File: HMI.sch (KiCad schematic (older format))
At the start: 42 parts, among them J24 Display, J25 SPI Interface, J26 I2C Interface, J27 LED4, J28 LED3, J29 Key 3, J30 Key 4, J31 Key 1, J32 Key 2, Q8 BC817, Q9 BC817, U9 74HC245

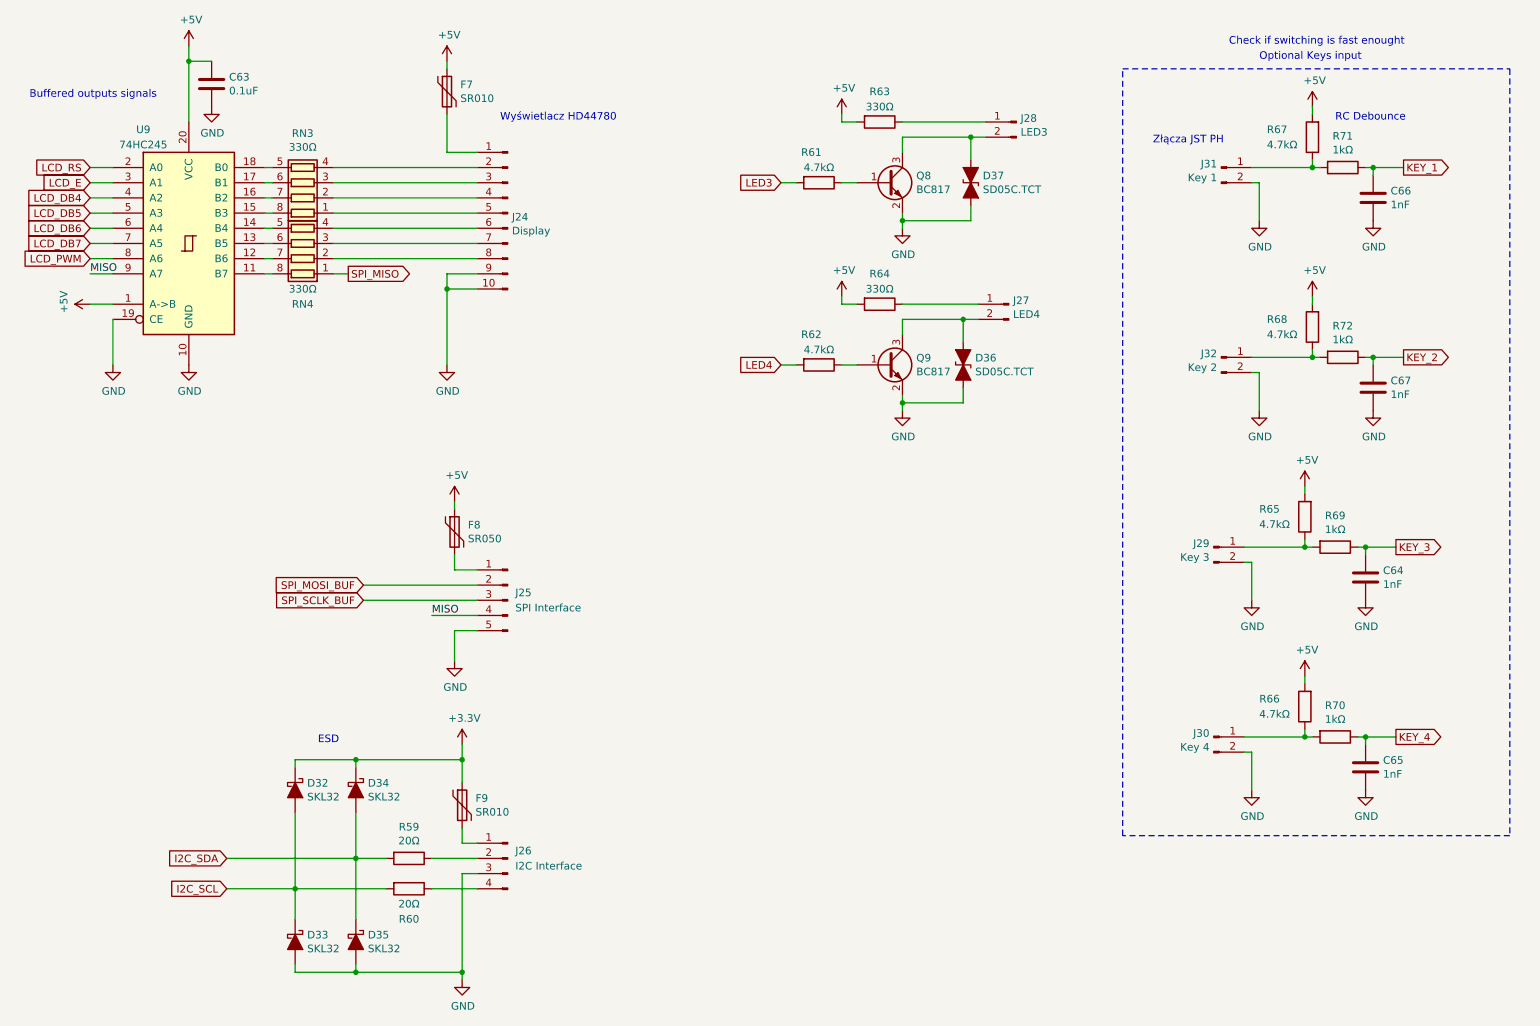
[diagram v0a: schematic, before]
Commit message: Added 12V regulator, aditional input, outputs, improved inputs ESD
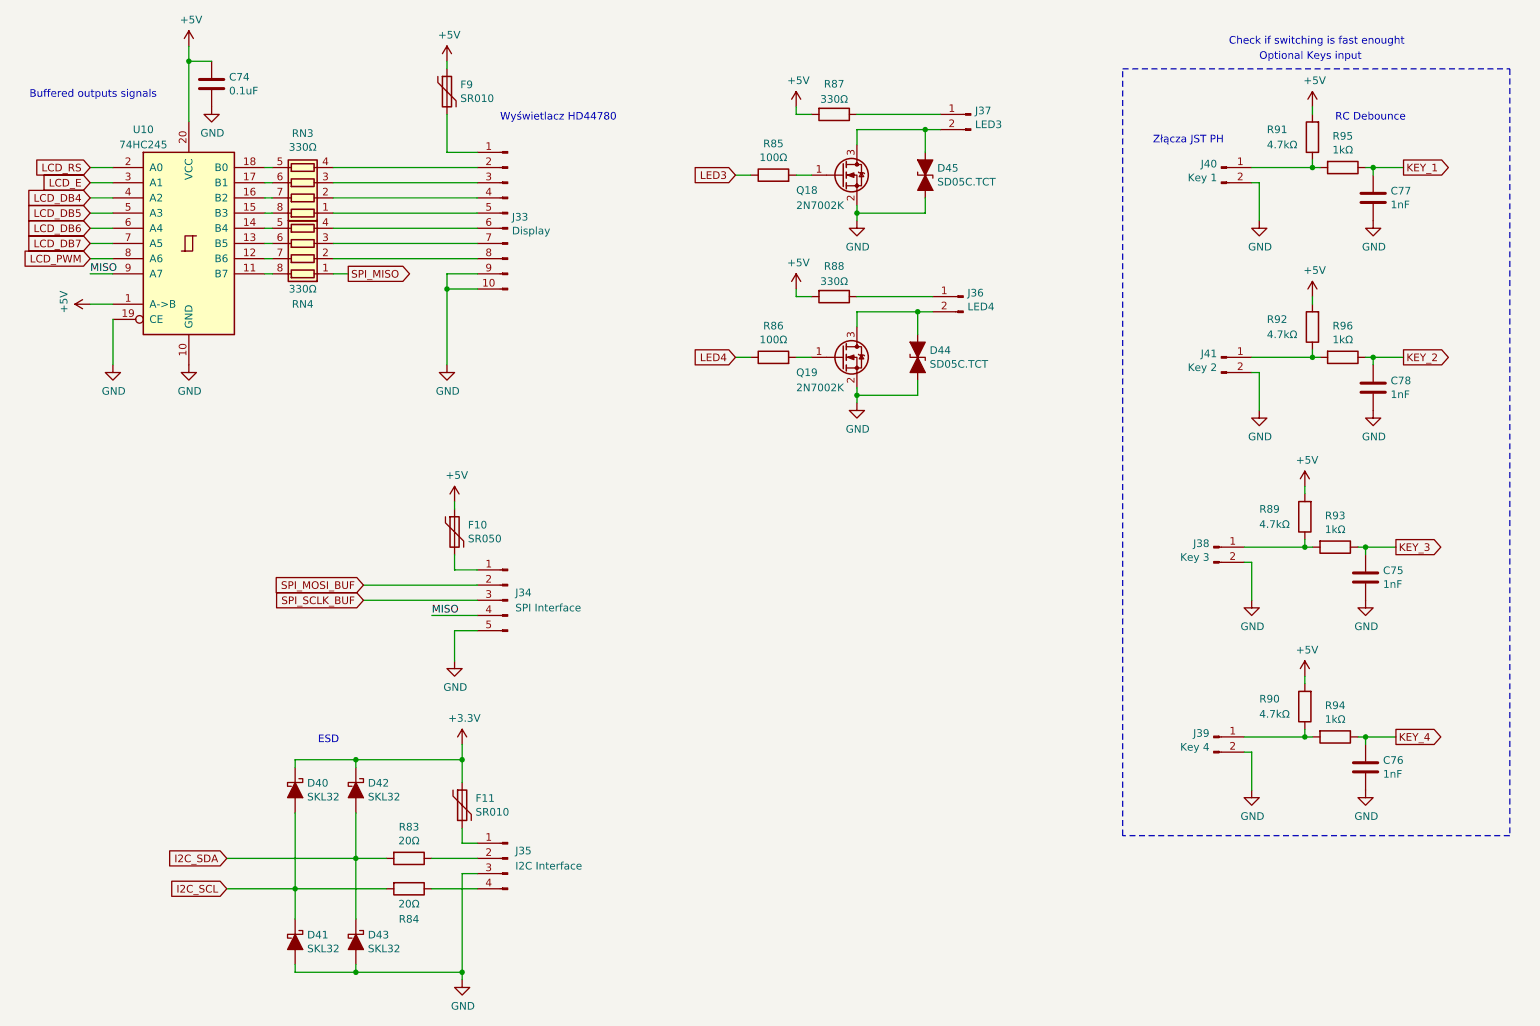
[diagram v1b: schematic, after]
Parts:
- removed Q8, Q9: BC817, Package_TO_SOT_SMD:SOT-23, symbol Transistor_BJT:BC817
- removed R61, R62: 4.7kΩ, Resistor_SMD:R_0603_1608Metric, symbol Device:R
- added Q18, Q19: 2N7002K, Package_TO_SOT_SMD:SOT-23, symbol Transistor_FET:2N7002K
- added R85, R86: 100Ω, Resistor_SMD:R_0603_1608Metric, symbol Device:R
- renumbered C63 to C74, C64 to C75, C65 to C76, C66 to C77, C67 to C78, D32 to D40, D33 to D41, D34 to D42, D35 to D43, D36 to D44, D37 to D45, F8 to F10, F9 to F11, F7 to F9, J24 to J33, J25 to J34, J26 to J35, J27 to J36, J28 to J37, J29 to J38, J30 to J39, J31 to J40, J32 to J41, R59 to R83, R60 to R84, R63 to R87, R64 to R88, R65 to R89, R66 to R90, R67 to R91, R68 to R92, R69 to R93, R70 to R94, R71 to R95, R72 to R96, U9 to U10
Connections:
- net GND: now also Q18.2 (S), Q19.2 (S)
- net LED3: now also R85.1
- net LED4: now also R86.1
- net at D45.1 (A1), J37.2 (Pin_2): now also Q18.3 (D)
- net at D44.1 (A1), J36.2 (Pin_2): now also Q19.3 (D)
- new net: Q19.1 (G), R86.2
- new net: Q18.1 (G), R85.2
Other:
- moved on the sheet: D44, D45, J36, J37, R87, R88

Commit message: Added analog input
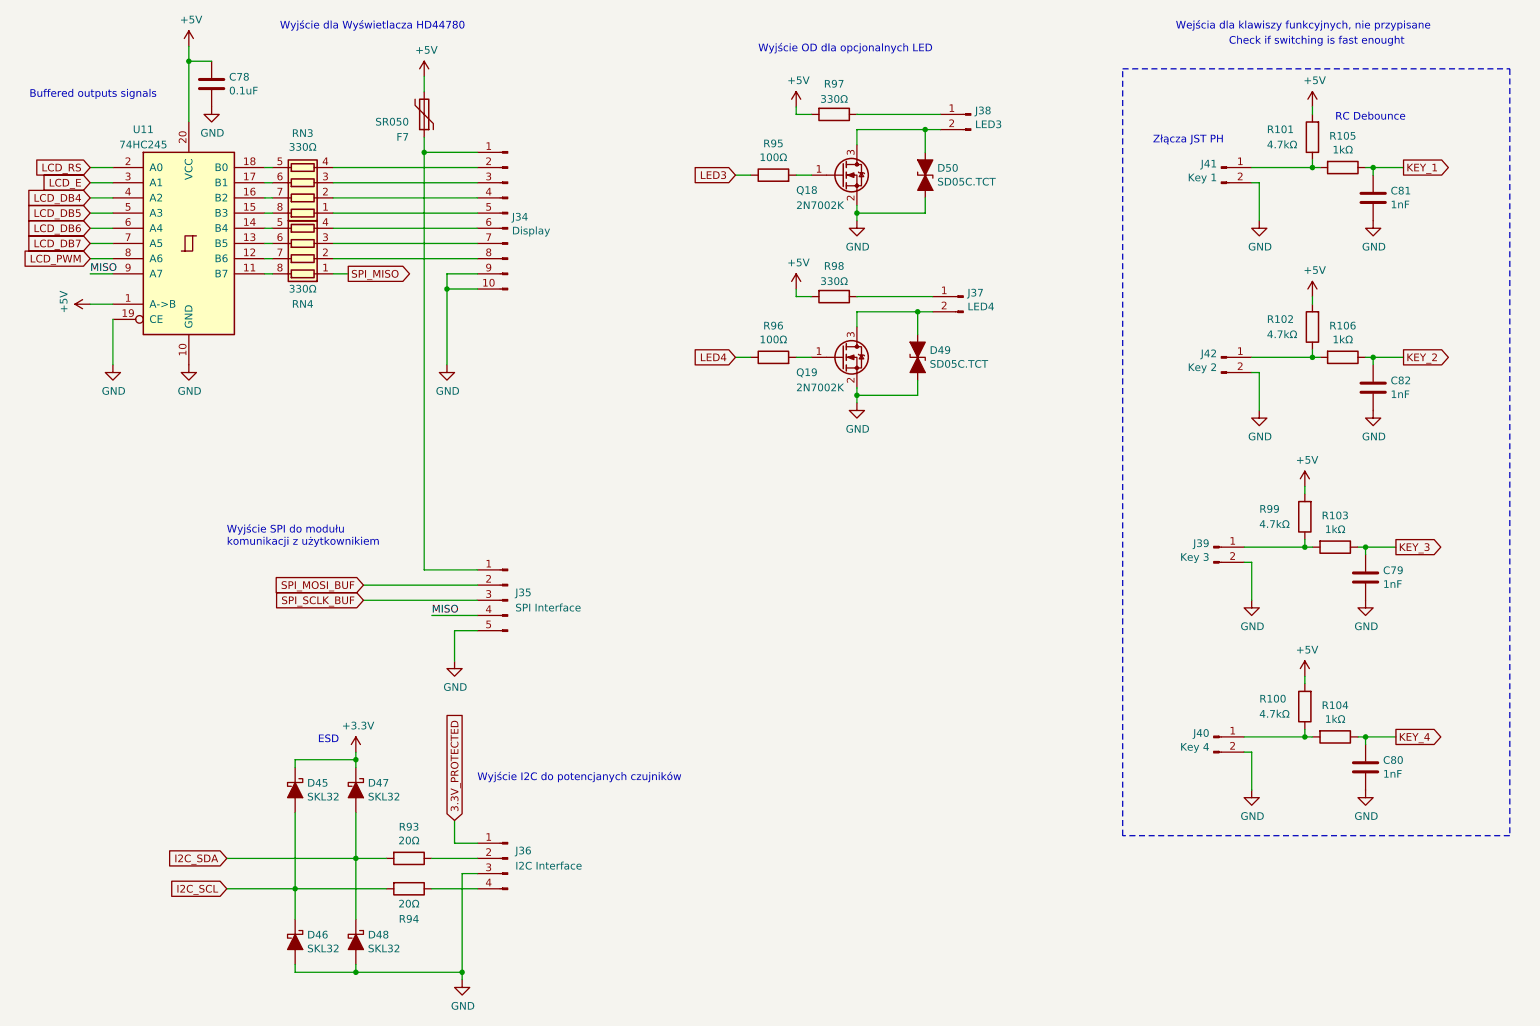
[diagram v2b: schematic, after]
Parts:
- removed F10: SR050, Fuse:Fuse_0805_2012Metric, symbol Device:Polyfuse
- removed F11, F9: SR010, Fuse:Fuse_0805_2012Metric, symbol Device:Polyfuse
- added F7: SR050, Fuse:Fuse_0805_2012Metric, symbol Device:Polyfuse
- renumbered C74 to C78, C75 to C79, C76 to C80, C77 to C81, C78 to C82, D40 to D45, D41 to D46, D42 to D47, D43 to D48, D44 to D49, D45 to D50, J33 to J34, J34 to J35, J35 to J36, J36 to J37, J37 to J38, J38 to J39, J39 to J40, J40 to J41, J41 to J42, R90 to R100, R91 to R101, R92 to R102, R93 to R103, R94 to R104, R95 to R105, R96 to R106, R83 to R93, R84 to R94, R85 to R95, R86 to R96, R87 to R97, R88 to R98, R89 to R99, U10 to U11
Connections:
- net +5V: now also F7.2
- net at J34.1 (Pin_1): now also J35.1 (Pin_1), F7.1
- net 3.3V_PROTECTED: now reaches J36.1 (Pin_1)
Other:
- note added: "Wejścia dla klawiszy funkcyjnych, nie przypisane"
- note added: "Wyjście I2C do potencjanych czujników"
- note added: "Wyjście OD dla opcjonalnych LED"
- note added: "Wyjście SPI do modułu\nkomunikacji z użytkownikiem"
- note added: "Wyjście dla Wyświetlacza HD44780"
- note removed: "Optional Keys input"
- note removed: "Wyświetlacz HD44780"

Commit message: Improve ESD Protection for TMC2209, Fuses. Schematic ready v1
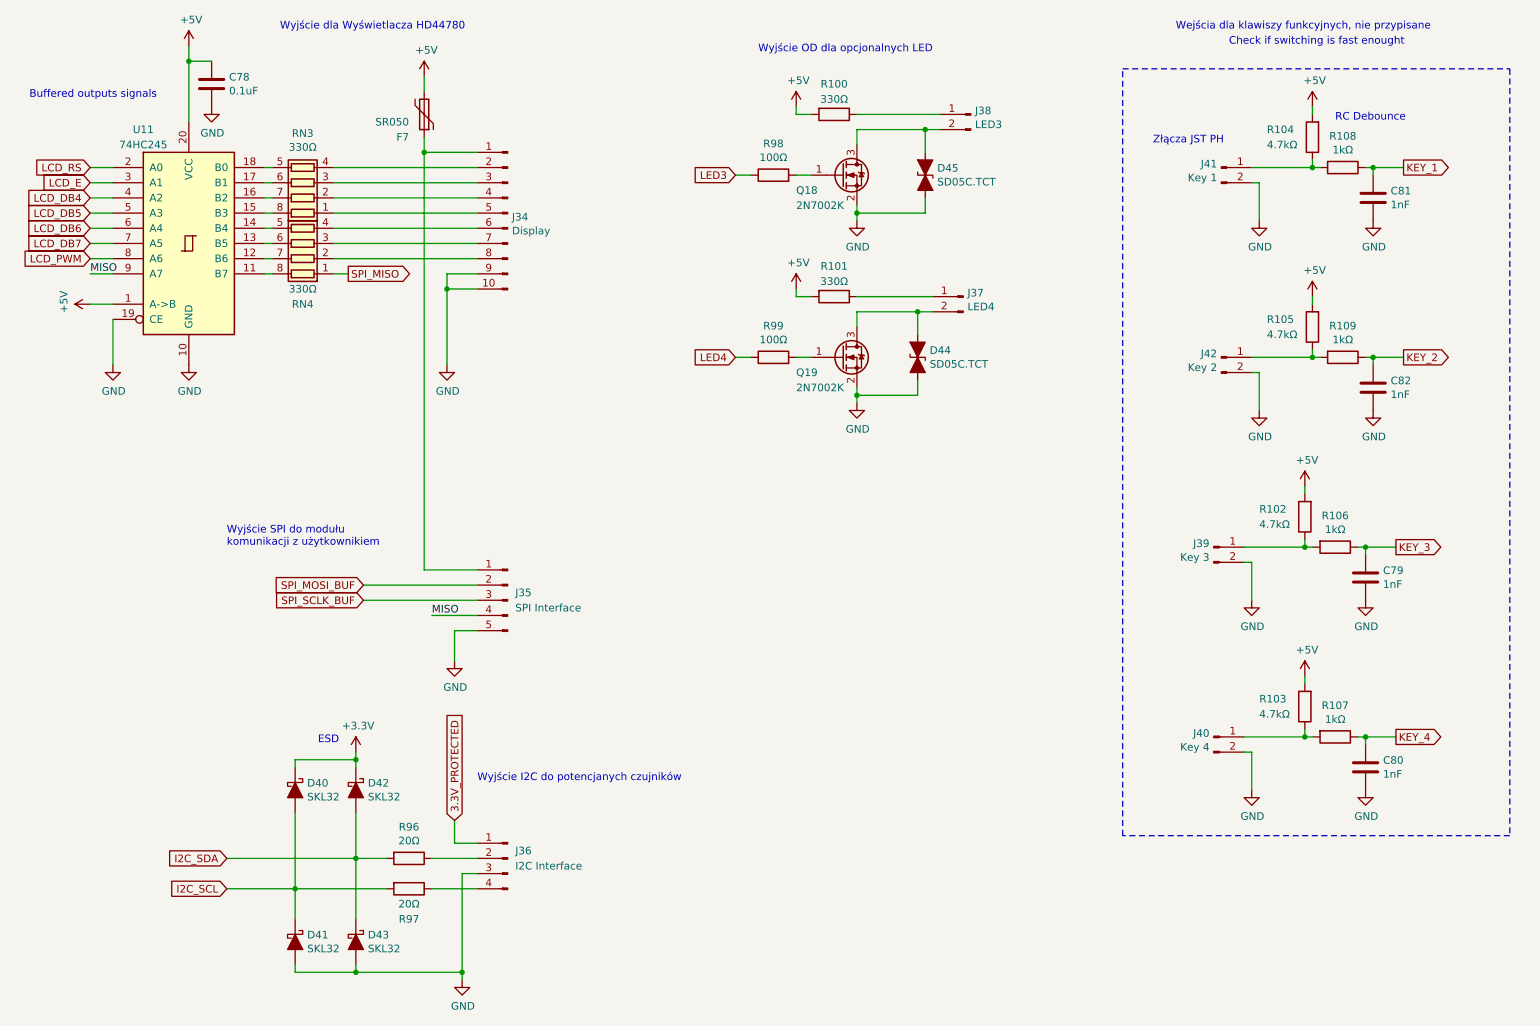
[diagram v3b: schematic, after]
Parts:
- renumbered D45 to D40, D46 to D41, D47 to D42, D48 to D43, D49 to D44, D50 to D45, R97 to R100, R98 to R101, R99 to R102, R100 to R103, R101 to R104, R102 to R105, R103 to R106, R104 to R107, R105 to R108, R106 to R109, R93 to R96, R94 to R97, R95 to R98, R96 to R99

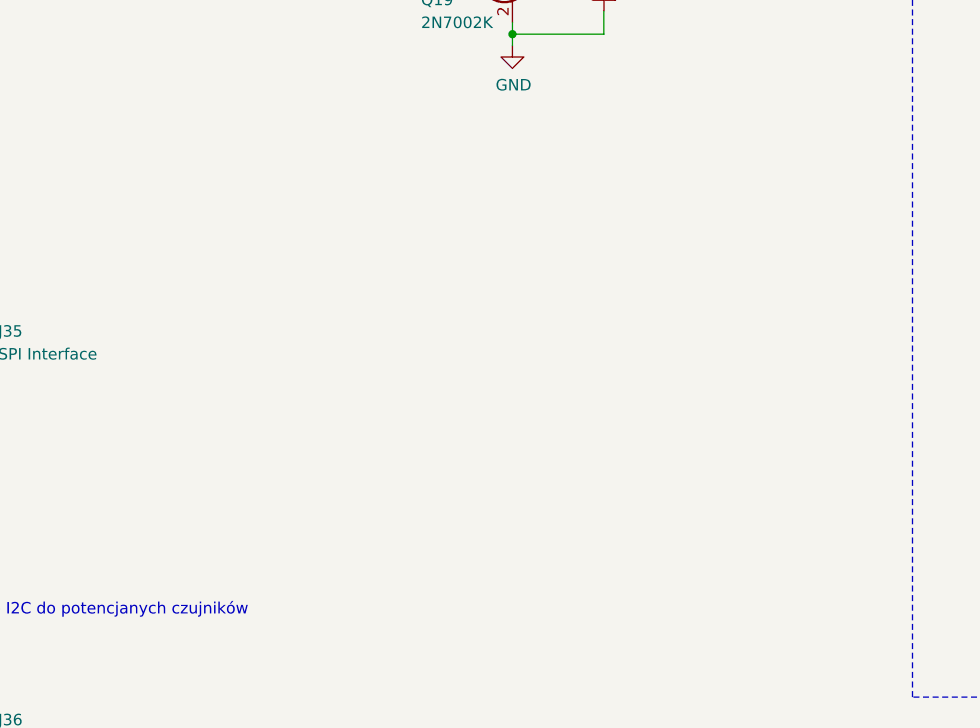
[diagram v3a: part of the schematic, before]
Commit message: Added rotary encoder input
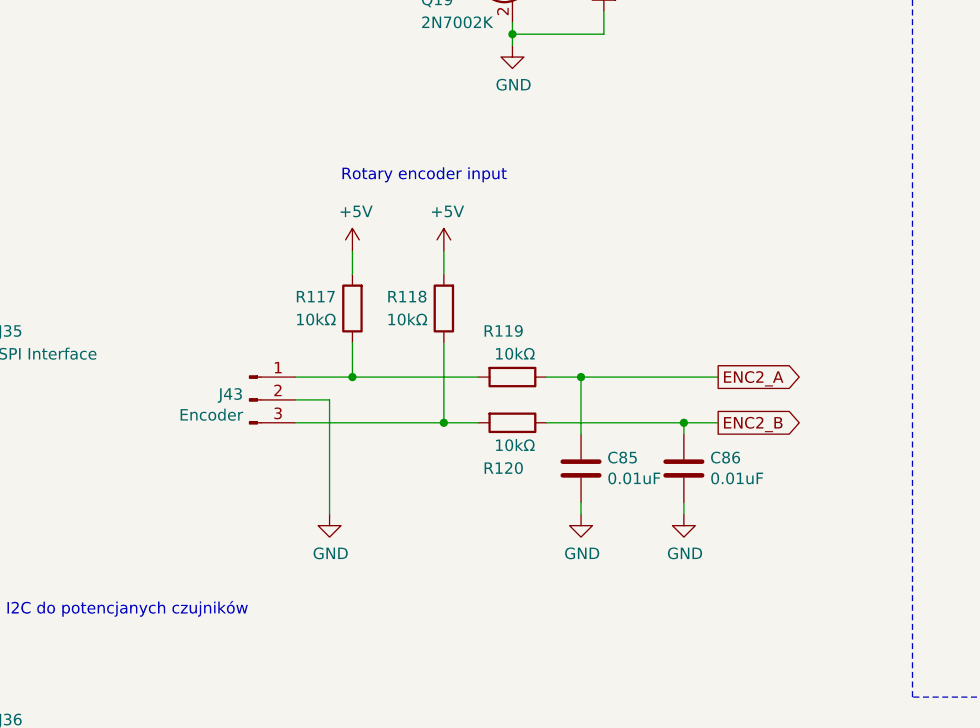
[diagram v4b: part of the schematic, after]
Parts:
- added C85, C86: 0.01uF, Capacitor_SMD:C_0603_1608Metric, symbol Device:C
- added J43: Encoder, Connector_JST:JST_PH_B3B-PH-K_1x03_P2.00mm_Vertical, symbol Connector:Conn_01x03_Male
- added R117, R118, R119, R120: 10kΩ, Resistor_SMD:R_0603_1608Metric, symbol Device:R
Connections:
- net +5V: now also R117.2, R118.2
- net GND: now also C85.2, C86.2, J43.2 (Pin_2)
- new net: J43.1 (Pin_1), R117.1, R119.2
- new net: J43.3 (Pin_3), R118.1, R120.2
- new net ENC2_A: C85.1, R119.1
- new net ENC2_B: C86.1, R120.1
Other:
- note added: "Rotary encoder input"

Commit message: Routing almost finished
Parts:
- added R47: 330Ω, Resistor_SMD:R_0603_1608Metric, symbol Device:R
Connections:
- net LCD_DB4: now also U11.7 (A5); no longer U11.4 (A2)
- net LCD_DB5: now also U11.6 (A4); no longer U11.5 (A3)
- net LCD_DB6: now also U11.5 (A3); no longer U11.6 (A4)
- net LCD_DB7: now also U11.4 (A2); no longer U11.7 (A5)
- net MISO: no longer J35.4 (Pin_4), U11.9 (A7)
- net SPI_MISO: now also R47.1; no longer RN4.1 (R1.1)
- net at U11.11 (B7): no longer RN4.8 (R1.2)
- new net: J35.4 (Pin_4), R47.2
- no-connect marks 0 -> 4
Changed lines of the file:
@@
 L power:+5V #PWR?
 U 1 1 5E132C10
-P 1450 2550
+P 1250 2550
 AR Path="/5E07245F/5E132C10" Ref="#PWR?"  Part="1"
 AR Path="/5E858220/5E132C10" Ref="#PWR?"  Part="1"
 AR Path="/5E91D96F/5E132C10" Ref="#PWR0181"  Part="1"
-F 0 "#PWR0181" H 1450 2400 50  0001 C CNN
-F 1 "+5V" H 1465 2723 50  0000 C CNN
-F 2 "" H 1450 2550 50  0001 C CNN
-F 3 "" H 1450 2550 50  0001 C CNN
-	1    1450 2550
+F 0 "#PWR0181" H 1250 2400 50  0001 C CNN
+F 1 "+5V" H 1265 2723 50  0000 C CNN
+F 2 "" H 1250 2550 50  0001 C CNN
+F 3 "" H 1250 2550 50  0001 C CNN
+	1    1250 2550
 	0    -1   -1   0
 $EndComp
 Wire Wire Line
-	1450 2550 1600 2550
+	1250 2550 1600 2550
 $Comp
 L Device:R_Pack04 RN?
@@
 Wire Wire Line
 	2600 2150 2650 2150
-Wire Wire Line
-	2600 2350 2650 2350
 Text Notes 1050 1200 0    50   ~ 0
 Buffered outputs signals
+Text GLabel 1450 2150 0    50   Input ~ 0
+LCD_DB4
+Text GLabel 1450 2050 0    50   Input ~ 0
+LCD_DB5
+Text GLabel 1450 1950 0    50   Input ~ 0
+LCD_DB6
 Text GLabel 1450 1850 0    50   Input ~ 0
-LCD_DB4
-Text GLabel 1450 1950 0    50   Input ~ 0
-LCD_DB5
-Text GLabel 1450 2050 0    50   Input ~ 0
-LCD_DB6
-Text GLabel 1450 2150 0    50   Input ~ 0
 LCD_DB7
 Text GLabel 1450 1750 0    50   Input ~ 0
@@
 	-1   0    0    -1
 $EndComp
-Text GLabel 3150 2350 2    50   Output ~ 0
+Text GLabel 3250 4600 0    50   Output ~ 0
 SPI_MISO
 $Comp
@@
 Wire Wire Line
 	3850 4700 3850 4900
-Wire Wire Line
-	4000 4600 3700 4600
-Text Label 3700 4600 0    50   ~ 0
+Text Label 1750 3650 0    50   ~ 0
 MISO
-Text Label 1450 2350 0    50   ~ 0
-MISO
-Wire Wire Line
-	1600 2350 1450 2350
 $Comp
 L power:GND #PWR?
@@
 $EndComp
 Wire Wire Line
-	3050 2350 3150 2350
-Wire Wire Line
 	2600 2250 2650 2250
 Wire Wire Line
@@
 Text Notes 5750 3800 0    50   ~ 0
 Rotary encoder input
+NoConn ~ 2600 2350
+NoConn ~ 2650 2350
+NoConn ~ 3050 2350
+NoConn ~ 1600 2350
+$Comp
+L Device:R R?
+U 1 1 5E330DF5
+P 3450 4600
+AR Path="/5E07245F/5E330DF5" Ref="R?"  Part="1"
+AR Path="/5E858220/5E330DF5" Ref="R?"  Part="1"
+AR Path="/5E91D96F/5E330DF5" Ref="R47"  Part="1"
+F 0 "R47" V 3250 4600 50  0000 C CNN
+F 1 "330Ω" V 3350 4600 50  0000 C CNN
+F 2 "Resistor_SMD:R_0603_1608Metric" V 3380 4600 50  0001 C CNN
+F 3 "~" H 3450 4600 50  0001 C CNN
+F 4 "0.04651" H 3450 4600 50  0001 C CNN "Cena"
+F 5 "SMD" H 3450 4600 50  0001 C CNN "Typ"
+	1    3450 4600
+	0    -1   -1   0
+$EndComp
+Wire Wire Line
+	3300 4600 3250 4600
+Wire Wire Line
+	3600 4600 4000 4600
 $EndSCHEMATC
